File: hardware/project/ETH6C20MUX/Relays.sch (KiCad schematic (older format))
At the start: 86 parts, among them J301 5499141-4, K301 HE3621A0510, K302 HE3621A0510, K303 HE3621A0510, K304 HE3621A0510, K305 HE3621A0510, K306 HE3621A0510, K307 HE3621A0510, K308 HE3621A0510, K309 HE3621A0510, K310 HE3621A0510, K311 HE3621A0510, K312 HE3621A0510, K313 HE3621A0510, K314 HE3621A0510, K315 HE3621A0510, K316 HE3621A0510, K317 HE3621A0510, K318 HE3621A0510, K319 HE3621A0510, K320 HE3621A0510, K321 HE3621A0510, K322 HE3621A0510, K323 HE3621A0510, K324 HE3621A0510, K325 HE3621A0510, K326 HE3621A0510, K327 HE3621A0510, K328 HE3621A0510, K329 HE3621A0510, K330 HE3621A0510, K331 HE3621A0510, K332 HE3621A0510, K333 HE3621A0510, K334 HE3621A0510, K335 HE3621A0510, K336 HE3621A0510, K337 HE3621A0510, K338 HE3621A0510, K339 HE3621A0510, K340 HE3621A0510, K341 HE3621A0510, K342 HE3621A0510, K343 HE3621A0510, K344 HE3621A0510, K345 HE3621A0510, K346 HE3621A0510, K347 HE3621A0510, K348 HE3621A0510, K349 HE3621A0510, K350 HE3621A0510, K351 HE3621A0510, K352 HE3621A0510, K353 HE3621A0510, K354 HE3621A0510, K355 HE3621A0510, K356 HE3621A0510, K357 HE3621A0510, K358 HE3621A0510, K359 HE3621A0510, K360 HE3621A0510, K361 HE3621A0510, K362 HE3621A0510, K363 HE3621A0510, K364 HE3621A0510, K365 HE3621A0510, K366 HE3621A0510, K367 HE3621A0510, K368 HE3621A0510, K369 HE3621A0510, K370 HE3621A0510, U301 MCZ33996, U302 MCZ33996, U303 MCZ33996, U304 MCZ33996, U305 MCZ33996

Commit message: PCB layout
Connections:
- net RELAY10A: now also U302.29 (OUT13); no longer U303.13 (OUT5)
- net RELAY10B: now also U303.15 (OUT6); no longer U303.12 (OUT4)
- net RELAY11A: now also U303.1 (OUT0); no longer U303.18 (OUT9)
- net RELAY11C: now also U303.29 (OUT13); no longer U303.21 (OUT11)
- net RELAY14C: no longer U301.15 (OUT6)
- net RELAY15A: no longer U301.18 (OUT9)
- net RELAY15B: no longer U301.20 (OUT10)
- net RELAY15C: no longer U301.21 (OUT11)
- net RELAY16A: now also U303.2 (OUT1); no longer U302.1 (OUT0)
- net RELAY16B: now also U303.18 (OUT9); no longer U302.2 (OUT1)
- net RELAY16C: now also U303.31 (OUT14); no longer U302.4 (OUT2)
- net RELAY17B: now also U303.16 (OUT7); no longer U302.29 (OUT13)
- net RELAY17C: now also U303.12 (OUT4); no longer U302.28 (OUT12)
- net RELAY18A: now also U302.12 (OUT4); no longer U303.15 (OUT6)
- net RELAY18B: now also U302.2 (OUT1); no longer U303.16 (OUT7)
- net RELAY18C: now also U302.18 (OUT9); no longer U303.17 (OUT8)
- net RELAY19A: now also U301.18 (OUT9); no longer U304.1 (OUT0)
- net RELAY19B: now also U301.32 (OUT15); no longer U304.2 (OUT1)
- net RELAY19C: now also U302.16 (OUT7); no longer U304.4 (OUT2)
- net RELAY1A: now also U301.16 (OUT7); no longer U301.1 (OUT0)
- net RELAY1B: now also U301.4 (OUT2); no longer U301.13 (OUT5)
- net RELAY1C: now also U301.17 (OUT8); no longer U301.32 (OUT15)
- net RELAY20A: now also U301.13 (OUT5); no longer U301.4 (OUT2)
- net RELAY20B: now also U301.12 (OUT4); no longer U301.5 (OUT3)
- net RELAY20C: now also U301.1 (OUT0); no longer U305.4 (OUT2)
- net RELAY2A: now also U301.21 (OUT11); no longer U302.16 (OUT7)
- net RELAY2B: now also U301.29 (OUT13); no longer U302.15 (OUT6)
- net RELAY2C: now also U302.13 (OUT5); no longer U302.17 (OUT8)
- net RELAY3A: now also U302.4 (OUT2); no longer U302.18 (OUT9)
- net RELAY3B: now also U302.17 (OUT8); no longer U302.20 (OUT10)
- net RELAY4A: now also U302.28 (OUT12); no longer U303.4 (OUT2)
- net RELAY4B: now also U303.13 (OUT5); no longer U303.2 (OUT1)
- net RELAY4C: now also U303.4 (OUT2); no longer U303.1 (OUT0)
- net RELAY5A: now also U303.17 (OUT8); no longer U303.31 (OUT14)
- net RELAY5B: now also U303.21 (OUT11); no longer U303.29 (OUT13)
- net RELAY7A: now also U301.15 (OUT6); no longer U301.2 (OUT1)
- net RELAY7B: now also U301.5 (OUT3); no longer U301.12 (OUT4)
- net RELAY7C: now also U301.2 (OUT1); no longer U301.31 (OUT14)
- net RELAY8A: now also U301.20 (OUT10); no longer U301.28 (OUT12)
- net RELAY8B: now also U301.31 (OUT14); no longer U301.17 (OUT8)
- net RELAY8C: now also U302.15 (OUT6); no longer U301.16 (OUT7)
- net RELAY9B: now also U302.1 (OUT0); no longer U302.12 (OUT4)
- net RELAY9C: now also U302.20 (OUT10); no longer U302.13 (OUT5)
- no-connect marks 14 -> 15
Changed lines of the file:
@@
 RELAYA
 Wire Wire Line
-	5000 1250 5450 1250
-Wire Wire Line
-	2700 1650 3150 1650
+	2700 4600 3150 4600
+Wire Wire Line
+	-750 1850 -300 1850
 Wire Wire Line
 	2700 5850 3150 5850
@@
 	5000 4300 5450 4300
 Wire Wire Line
-	2700 4300 3150 4300
+	2700 4500 3150 4500
 Wire Wire Line
 	2700 3500 3150 3500
 Wire Wire Line
-	5000 1550 5450 1550
-Text Label 5450 1250 2    50   ~ 0
+	5000 2050 5450 2050
+Text Label 3150 4600 2    50   ~ 0
 RELAY16C
-Text Label 3150 1650 2    50   ~ 0
+Text Label -300 1850 2    50   ~ 0
 RELAY14C
 Text Label 3150 5850 2    50   ~ 0
@@
 Text Label 5450 4300 2    50   ~ 0
 RELAY12C
-Text Label 3150 4300 2    50   ~ 0
+Text Label 3150 4500 2    50   ~ 0
 RELAY11C
 Text Label 3150 3500 2    50   ~ 0
 RELAY10C
-Text Label 5450 1550 2    50   ~ 0
+Text Label 5450 2050 2    50   ~ 0
 RELAY9C
 Wire Wire Line
-	5000 1150 5450 1150
+	2700 4100 3150 4100
 Wire Wire Line
 	2700 5450 3150 5450
@@
 	2700 4200 3150 4200
 Wire Wire Line
-	2700 3600 3150 3600
-Wire Wire Line
-	5000 1450 5450 1450
-Wire Wire Line
-	2700 1550 3150 1550
-Wire Wire Line
-	5000 1650 5450 1650
-Wire Wire Line
-	5000 2050 5450 2050
-Wire Wire Line
-	2700 3300 3150 3300
-Wire Wire Line
-	2700 4500 3150 4500
+	2700 3800 3150 3800
+Wire Wire Line
+	5000 1050 5450 1050
+Wire Wire Line
+	2700 1250 3150 1250
+Wire Wire Line
+	2700 2350 3150 2350
+Wire Wire Line
+	5000 1850 5450 1850
+Wire Wire Line
+	2700 3700 3150 3700
+Wire Wire Line
+	2700 4300 3150 4300
 Wire Wire Line
 	5000 4500 5450 4500
 Wire Wire Line
-	2700 1450 3150 1450
-Wire Wire Line
-	2700 1850 3150 1850
-Text Label 5450 1150 2    50   ~ 0
+	2700 2450 3150 2450
+Text Label 3150 4100 2    50   ~ 0
 RELAY16B
 Text Label 3150 5450 2    50   ~ 0
@@
 Text Label 3150 4200 2    50   ~ 0
 RELAY11B
-Text Label 3150 3600 2    50   ~ 0
+Text Label 3150 3800 2    50   ~ 0
 RELAY10B
-Text Label 5450 1450 2    50   ~ 0
+Text Label 5450 1050 2    50   ~ 0
 RELAY9B
-Text Label 3150 1850 2    50   ~ 0
+Text Label 3150 2450 2    50   ~ 0
 RELAY8B
-Text Label 3150 1450 2    50   ~ 0
-RELAY7B
 Text Label 5450 4500 2    50   ~ 0
 RELAY6B
-Text Label 3150 4500 2    50   ~ 0
+Text Label 3150 4300 2    50   ~ 0
 RELAY5B
-Text Label 3150 3300 2    50   ~ 0
+Text Label 3150 3700 2    50   ~ 0
 RELAY4B
-Text Label 5450 2050 2    50   ~ 0
+Text Label 5450 1850 2    50   ~ 0
 RELAY3B
+Text Label 3150 2350 2    50   ~ 0
+RELAY2B
+Text Label 3150 1250 2    50   ~ 0
+RELAY1B
+Wire Wire Line
+	2700 3400 3150 3400
+Wire Wire Line
+	2700 4400 3150 4400
+Wire Wire Line
+	5000 4600 5450 4600
+Wire Wire Line
+	2700 1150 3150 1150
+Wire Wire Line
+	5000 1650 5450 1650
 Text Label 5450 1650 2    50   ~ 0
-RELAY2B
-Text Label 3150 1550 2    50   ~ 0
-RELAY1B
-Wire Wire Line
-	2700 3200 3150 3200
-Wire Wire Line
-	2700 4400 3150 4400
-Wire Wire Line
-	5000 4600 5450 4600
-Wire Wire Line
-	2700 2450 3150 2450
-Wire Wire Line
-	2700 1750 3150 1750
-Text Label 3150 1750 2    50   ~ 0
 RELAY8C
-Text Label 3150 2450 2    50   ~ 0
+Text Label 3150 1150 2    50   ~ 0
 RELAY7C
 Text Label 5450 4600 2    50   ~ 0
@@
 Text Label 3150 4400 2    50   ~ 0
 RELAY5C
-Text Label 3150 3200 2    50   ~ 0
+Text Label 3150 3400 2    50   ~ 0
 RELAY4C
 Wire Wire Line
-	5000 1050 5450 1050
-Wire Wire Line
 	2700 5350 3150 5350
 Wire Wire Line
@@
 	5000 4100 5450 4100
 Wire Wire Line
-	2700 4100 3150 4100
-Wire Wire Line
-	2700 3700 3150 3700
+	2700 3200 3150 3200
+Wire Wire Line
+	5000 2350 5450 2350
 Wire Wire Line
 	5000 1350 5450 1350
 Wire Wire Line
-	2700 1050 3150 1050
-Wire Wire Line
-	5000 1750 5450 1750
-Wire Wire Line
-	5000 1950 5450 1950
-Wire Wire Line
-	2700 3400 3150 3400
-Wire Wire Line
-	2700 4600 3150 4600
+	2700 1750 3150 1750
+Wire Wire Line
+	2700 2150 3150 2150
+Wire Wire Line
+	5000 1250 5450 1250
+Wire Wire Line
+	5000 2250 5450 2250
+Wire Wire Line
+	2700 4000 3150 4000
 Wire Wire Line
 	5000 4400 5450 4400
 Wire Wire Line
-	2700 1150 3150 1150
-Wire Wire Line
-	2700 2250 3150 2250
-Text Label 5450 1050 2    50   ~ 0
-RELAY16A
+	2700 1650 3150 1650
+Wire Wire Line
+	2700 2050 3150 2050
 Text Label 3150 5350 2    50   ~ 0
 RELAY14A
@@
 Text Label 5450 4100 2    50   ~ 0
 RELAY12A
-Text Label 3150 4100 2    50   ~ 0
+Text Label 3150 3200 2    50   ~ 0
 RELAY11A
-Text Label 3150 3700 2    50   ~ 0
+Text Label 5450 2350 2    50   ~ 0
 RELAY10A
 Text Label 5450 1350 2    50   ~ 0
 RELAY9A
-Text Label 3150 2250 2    50   ~ 0
+Text Label 3150 2050 2    50   ~ 0
 RELAY8A
-Text Label 3150 1150 2    50   ~ 0
+Text Label 3150 1650 2    50   ~ 0
 RELAY7A
 Text Label 5450 4400 2    50   ~ 0
 RELAY6A
-Text Label 3150 4600 2    50   ~ 0
+Text Label 3150 4000 2    50   ~ 0
 RELAY5A
-Text Label 3150 3400 2    50   ~ 0
+Text Label 5450 2250 2    50   ~ 0
 RELAY4A
-Text Label 5450 1950 2    50   ~ 0
+Text Label 5450 1250 2    50   ~ 0
 RELAY3A
-Text Label 5450 1750 2    50   ~ 0
+Text Label 3150 2150 2    50   ~ 0
 RELAY2A
-Text Label 3150 1050 2    50   ~ 0
+Text Label 3150 1750 2    50   ~ 0
 RELAY1A
 Wire Wire Line
@@
 Wire Wire Line
 	8200 4950 8200 5350
-Text Label 3150 2550 2    50   ~ 0
+Text Label 3150 1850 2    50   ~ 0
 RELAY1C
-Text Label 5450 1850 2    50   ~ 0
+Text Label 5450 1550 2    50   ~ 0
 RELAY2C
 Text Label 5450 2150 2    50   ~ 0
@@
 	5000 2150 5450 2150
 Wire Wire Line
-	5000 1850 5450 1850
-Wire Wire Line
-	2700 2550 3150 2550
+	5000 1550 5450 1550
+Wire Wire Line
+	2700 1850 3150 1850
 NoConn ~ 5000 2550
 NoConn ~ 2700 4700
 Wire Wire Line
-	5000 2250 5450 2250
-Text Label 5450 2250 2    50   ~ 0
+	2700 3600 3150 3600
+Text Label 3150 3600 2    50   ~ 0
 RELAY17C
 Wire Wire Line
-	5000 2350 5450 2350
-Text Label 5450 2350 2    50   ~ 0
+	2700 3900 3150 3900
+Text Label 3150 3900 2    50   ~ 0
 RELAY17B
 Wire Wire Line
@@
 RELAY17A
 Wire Wire Line
-	2700 4000 3150 4000
-Text Label 3150 4000 2    50   ~ 0
+	5000 1950 5450 1950
+Text Label 5450 1950 2    50   ~ 0
 RELAY18C
 Wire Wire Line
-	2700 3900 3150 3900
-Text Label 3150 3900 2    50   ~ 0
+	5000 1150 5450 1150
+Text Label 5450 1150 2    50   ~ 0
 RELAY18B
 Wire Wire Line
-	2700 3800 3150 3800
-Text Label 3150 3800 2    50   ~ 0
+	5000 1450 5450 1450
+Text Label 5450 1450 2    50   ~ 0
 RELAY18A
 Wire Wire Line
-	5000 3400 5450 3400
-Text Label 5450 3400 2    50   ~ 0
+	5000 1750 5450 1750
+Text Label 5450 1750 2    50   ~ 0
 RELAY19C
 Wire Wire Line
-	5000 3300 5450 3300
-Text Label 5450 3300 2    50   ~ 0
+	2700 2550 3150 2550
+Text Label 3150 2550 2    50   ~ 0
 RELAY19B
 Wire Wire Line
-	5000 3200 5450 3200
-Text Label 5450 3200 2    50   ~ 0
+	2700 1950 3150 1950
+Text Label 3150 1950 2    50   ~ 0
 RELAY19A
 Wire Wire Line
-	2700 5550 3150 5550
-Text Label 3150 5550 2    50   ~ 0
+	2700 1050 3150 1050
+Text Label 3150 1050 2    50   ~ 0
 RELAY20C
 Wire Wire Line
-	2700 1350 3150 1350
-Text Label 3150 1350 2    50   ~ 0
+	2700 1450 3150 1450
+Text Label 3150 1450 2    50   ~ 0
 RELAY20B
 Wire Wire Line
-	2700 1250 3150 1250
-Text Label 3150 1250 2    50   ~ 0
+	2700 1550 3150 1550
+Text Label 3150 1550 2    50   ~ 0
 RELAY20A
 Wire Wire Line
@@
 Text Label 11450 10100 2    50   ~ 0
 PIN20
-Text Label 3150 1950 2    50   ~ 0
+Text Label -300 2150 2    50   ~ 0
 RELAY15A
 Wire Wire Line
-	2700 1950 3150 1950
-Text Label 3150 2050 2    50   ~ 0
+	-750 2150 -300 2150
+Text Label -300 2250 2    50   ~ 0
 RELAY15B
 Wire Wire Line
-	2700 2050 3150 2050
-Text Label 3150 2150 2    50   ~ 0
+	-750 2250 -300 2250
+Text Label -300 2350 2    50   ~ 0
 RELAY15C
 Wire Wire Line
-	2700 2150 3150 2150
+	-750 2350 -300 2350
 NoConn ~ 5000 3500
 NoConn ~ 5000 3600
@@
 Wire Wire Line
 	2700 6850 3150 6850
+Text Label 3150 1350 2    50   ~ 0
+RELAY7B
+Wire Wire Line
+	2700 1350 3150 1350
+NoConn ~ 2700 2250
+Text Label 3150 3300 2    50   ~ 0
+RELAY16A
+Wire Wire Line
+	2700 3300 3150 3300
 $EndSCHEMATC

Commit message: Main PCB layout done
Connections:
- net RELAY10A: now also U303.28 (OUT12); no longer U302.29 (OUT13)
- net RELAY10B: now also U303.21 (OUT11); no longer U303.15 (OUT6)
- net RELAY10C: now also U303.20 (OUT10); no longer U303.5 (OUT3)
- net RELAY11A: now also U303.18 (OUT9); no longer U303.1 (OUT0)
- net RELAY11B: now also U304.15 (OUT6); no longer U303.20 (OUT10)
- net RELAY11C: now also U304.13 (OUT5); no longer U303.29 (OUT13)
- net RELAY12A: now also U304.12 (OUT4); no longer U304.18 (OUT9)
- net RELAY12B: now also U304.5 (OUT3); no longer U304.20 (OUT10)
- net RELAY12C: now also U304.4 (OUT2); no longer U304.21 (OUT11)
- net RELAY13A: now also U305.17 (OUT8); no longer U305.5 (OUT3)
- net RELAY13B: now also U305.15 (OUT6); no longer U305.12 (OUT4)
- net RELAY14A: now also U305.16 (OUT7); no longer U305.1 (OUT0)
- net RELAY14B: now also U305.29 (OUT13); no longer U305.2 (OUT1)
- net RELAY14C: now also U305.31 (OUT14)
- net RELAY15A: now also U304.31 (OUT14)
- net RELAY15B: now also U304.32 (OUT15)
- net RELAY15C: now also U304.16 (OUT7)
- net RELAY16A: now also U303.4 (OUT2); no longer U303.2 (OUT1)
- net RELAY16B: now also U304.28 (OUT12); no longer U303.18 (OUT9)
- net RELAY16C: now also U304.29 (OUT13); no longer U303.31 (OUT14)
- net RELAY17A: now also U303.13 (OUT5); no longer U302.31 (OUT14)
- net RELAY17B: now also U303.12 (OUT4); no longer U303.16 (OUT7)
- net RELAY17C: now also U303.5 (OUT3); no longer U303.12 (OUT4)
- net RELAY18A: now also U302.32 (OUT15); no longer U302.12 (OUT4)
- net RELAY18B: now also U302.31 (OUT14); no longer U302.2 (OUT1)
- net RELAY18C: now also U303.15 (OUT6); no longer U302.18 (OUT9)
- net RELAY19A: now also U302.4 (OUT2); no longer U301.18 (OUT9)
- net RELAY19B: now also U302.29 (OUT13); no longer U301.32 (OUT15)
- net RELAY19C: now also U302.28 (OUT12); no longer U302.16 (OUT7)
- net RELAY1B: now also U301.1 (OUT0); no longer U301.4 (OUT2)
- net RELAY1C: now also U301.28 (OUT12); no longer U301.17 (OUT8)
- net RELAY20B: now also U301.4 (OUT2); no longer U301.12 (OUT4)
- net RELAY20C: now also U301.31 (OUT14); no longer U301.1 (OUT0)
- net RELAY2A: now also U301.32 (OUT15); no longer U301.21 (OUT11)
- net RELAY2B: now also U302.1 (OUT0); no longer U301.29 (OUT13)
- net RELAY2C: now also U302.21 (OUT11); no longer U302.13 (OUT5)
- net RELAY3A: now also U303.1 (OUT0); no longer U302.4 (OUT2)
- net RELAY3B: now also U303.2 (OUT1); no longer U302.17 (OUT8)
- net RELAY3C: now also U303.16 (OUT7); no longer U302.21 (OUT11)
- net RELAY4A: now also U303.32 (OUT15); no longer U302.28 (OUT12)
- net RELAY4B: now also U303.31 (OUT14); no longer U303.13 (OUT5)
- net RELAY4C: now also U303.29 (OUT13); no longer U303.4 (OUT2)
- net RELAY5A: now also U304.1 (OUT0); no longer U303.17 (OUT8)
- net RELAY5B: now also U304.2 (OUT1); no longer U303.21 (OUT11)
- net RELAY5C: now also U304.17 (OUT8); no longer U303.28 (OUT12)
- net RELAY6A: now also U304.18 (OUT9); no longer U304.28 (OUT12)
- net RELAY6B: now also U304.20 (OUT10); no longer U304.29 (OUT13)
- net RELAY6C: now also U304.21 (OUT11); no longer U304.31 (OUT14)
- net RELAY7B: now also U301.2 (OUT1); no longer U301.5 (OUT3)
- net RELAY7C: now also U301.29 (OUT13); no longer U301.2 (OUT1)
- net RELAY8A: now also U302.2 (OUT1); no longer U301.20 (OUT10)
- net RELAY8B: now also U302.13 (OUT5); no longer U301.31 (OUT14)
- net RELAY8C: now also U302.12 (OUT4); no longer U302.15 (OUT6)
- net RELAY9A: now also U302.16 (OUT7); no longer U302.5 (OUT3)
- net RELAY9B: now also U302.15 (OUT6); no longer U302.1 (OUT0)
- net RELAY9C: now also U303.17 (OUT8); no longer U302.20 (OUT10)
- net RELAYA: now also U305.21 (OUT11); no longer U305.31 (OUT14)
- net RELAYAB: now also U305.20 (OUT10); no longer U305.17 (OUT8)
- net RELAYB: now also U305.28 (OUT12); no longer U305.29 (OUT13)
- net RELAYBA: now also U305.1 (OUT0); no longer U305.15 (OUT6)
- net RELAYC: now also U305.32 (OUT15); no longer U305.28 (OUT12)
- net RELAYD: now also U305.12 (OUT4); no longer U305.21 (OUT11)
- net RELAYE: now also U305.5 (OUT3); no longer U305.20 (OUT10)
- net RELAYEA: now also U305.18 (OUT9); no longer U305.16 (OUT7)
- net RELAYF: now also U305.4 (OUT2); no longer U305.18 (OUT9)
- net RELAYFA: now also U305.2 (OUT1); no longer U305.32 (OUT15)

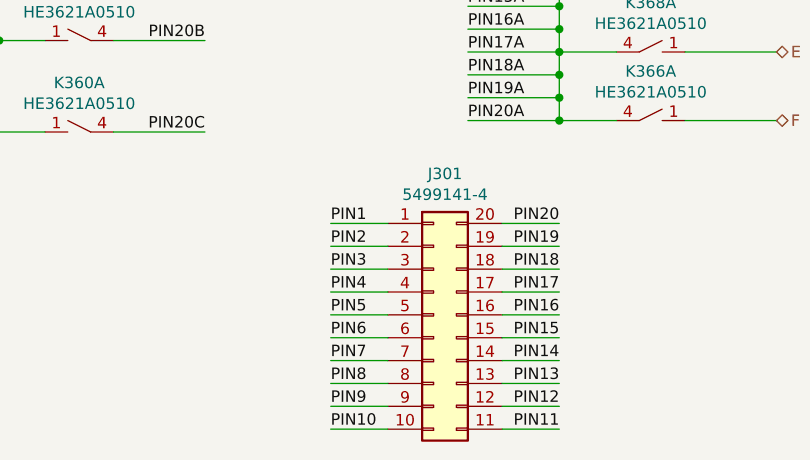
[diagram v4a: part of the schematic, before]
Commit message: PCB main and module layout.
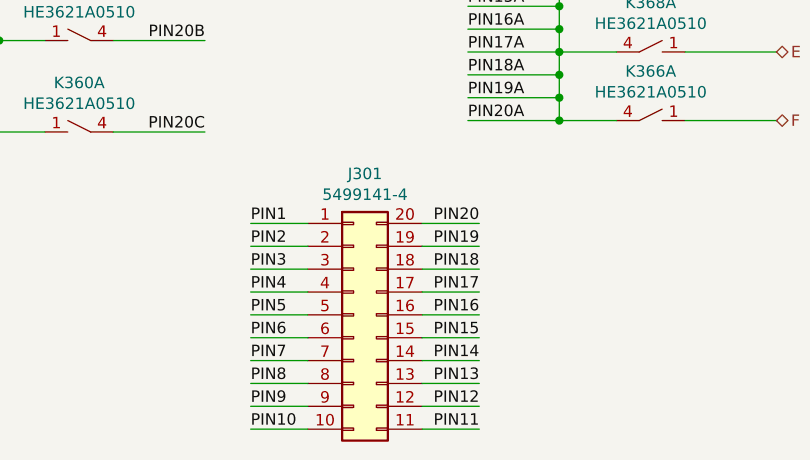
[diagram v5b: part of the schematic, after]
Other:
- moved on the sheet: J301
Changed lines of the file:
@@
 $EndDescr
 Wire Wire Line
-	10700 10100 10450 10100
+	10350 10100 10100 10100
 Wire Wire Line
-	10700 10200 10450 10200
+	10350 10200 10100 10200
 Wire Wire Line
-	10700 10300 10450 10300
+	10350 10300 10100 10300
 Wire Wire Line
-	10700 10400 10450 10400
+	10350 10400 10100 10400
 Wire Wire Line
-	10700 10500 10450 10500
+	10350 10500 10100 10500
 Wire Wire Line
-	10700 10600 10450 10600
+	10350 10600 10100 10600
 Wire Wire Line
-	10700 10700 10450 10700
+	10350 10700 10100 10700
 Wire Wire Line
-	10700 10800 10450 10800
+	10350 10800 10100 10800
 Wire Wire Line
-	10700 10900 10450 10900
+	10350 10900 10100 10900
 Wire Wire Line
-	10700 11000 10450 11000
+	10350 11000 10100 11000
 Wire Wire Line
-	11200 11000 11450 11000
+	10850 11000 11100 11000
 Wire Wire Line
-	11200 10900 11450 10900
+	10850 10900 11100 10900
 Wire Wire Line
-	11200 10800 11450 10800
+	10850 10800 11100 10800
 Wire Wire Line
-	11200 10700 11450 10700
+	10850 10700 11100 10700
 Wire Wire Line
-	11200 10600 11450 10600
+	10850 10600 11100 10600
 Wire Wire Line
-	11200 10500 11450 10500
-Text Label 10450 10100 0    50   ~ 0
+	10850 10500 11100 10500
+Text Label 10100 10100 0    50   ~ 0
 PIN1
-Text Label 10450 10200 0    50   ~ 0
+Text Label 10100 10200 0    50   ~ 0
 PIN2
-Text Label 10450 10300 0    50   ~ 0
+Text Label 10100 10300 0    50   ~ 0
 PIN3
-Text Label 10450 10400 0    50   ~ 0
+Text Label 10100 10400 0    50   ~ 0
 PIN4
-Text Label 10450 10500 0    50   ~ 0
+Text Label 10100 10500 0    50   ~ 0
 PIN5
-Text Label 10450 10600 0    50   ~ 0
+Text Label 10100 10600 0    50   ~ 0
 PIN6
-Text Label 10450 10700 0    50   ~ 0
+Text Label 10100 10700 0    50   ~ 0
 PIN7
-Text Label 10450 10800 0    50   ~ 0
+Text Label 10100 10800 0    50   ~ 0
 PIN8
-Text Label 10450 10900 0    50   ~ 0
+Text Label 10100 10900 0    50   ~ 0
 PIN9
-Text Label 10450 11000 0    50   ~ 0
+Text Label 10100 11000 0    50   ~ 0
 PIN10
-Text Label 11450 11000 2    50   ~ 0
+Text Label 11100 11000 2    50   ~ 0
 PIN11
-Text Label 11450 10900 2    50   ~ 0
+Text Label 11100 10900 2    50   ~ 0
 PIN12
-Text Label 11450 10800 2    50   ~ 0
+Text Label 11100 10800 2    50   ~ 0
 PIN13
-Text Label 11450 10700 2    50   ~ 0
+Text Label 11100 10700 2    50   ~ 0
 PIN14
-Text Label 11450 10600 2    50   ~ 0
+Text Label 11100 10600 2    50   ~ 0
 PIN15
-Text Label 11450 10500 2    50   ~ 0
+Text Label 11100 10500 2    50   ~ 0
 PIN16
 Wire Wire Line
@@
 L Connector_Generic:Conn_02x10_Counter_Clockwise J301
 U 1 1 6554E0B3
-P 10900 10500
-F 0 "J301" H 10950 11117 50  0000 C CNN
-F 1 "5499141-4" H 10950 11026 50  0000 C CNN
-F 2 "Connector_IDC:IDC-Header_2x10_P2.54mm_Horizontal_Lock" H 10900 10500 50  0001 C CNN
-F 3 "~" H 10900 10500 50  0001 C CNN
-	1    10900 10500
+P 10550 10500
+F 0 "J301" H 10600 11117 50  0000 C CNN
+F 1 "5499141-4" H 10600 11026 50  0000 C CNN
+F 2 "Connector_IDC:IDC-Header_2x10_P2.54mm_Horizontal_Lock" H 10550 10500 50  0001 C CNN
+F 3 "~" H 10550 10500 50  0001 C CNN
+	1    10550 10500
 	1    0    0    -1
 $EndComp
 Wire Wire Line
-	11200 10400 11450 10400
-Text Label 11450 10400 2    50   ~ 0
+	10850 10400 11100 10400
+Text Label 11100 10400 2    50   ~ 0
 PIN17
 Wire Wire Line
-	11200 10300 11450 10300
-Text Label 11450 10300 2    50   ~ 0
+	10850 10300 11100 10300
+Text Label 11100 10300 2    50   ~ 0
 PIN18
 Wire Wire Line
-	11200 10200 11450 10200
-Text Label 11450 10200 2    50   ~ 0
+	10850 10200 11100 10200
+Text Label 11100 10200 2    50   ~ 0
 PIN19
 Wire Wire Line
-	11200 10100 11450 10100
-Text Label 11450 10100 2    50   ~ 0
+	10850 10100 11100 10100
+Text Label 11100 10100 2    50   ~ 0
 PIN20
 Text Label 5450 4700 2    50   ~ 0
